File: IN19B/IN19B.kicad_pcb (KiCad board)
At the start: 2 copper layers, 18 x 18 mm, 16 parts

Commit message: Add files via upload
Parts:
- moved H 0.49 mm to (74.0, 106.6), turned to 31 degrees
- moved V 0.27 mm to (72.4, 104.6), turned to 51 degrees
- moved S 0.23 mm to (73.7, 115.2), turned to 321 degrees
- moved F 0.10 mm to (74.8, 113.0), turned to 342 degrees
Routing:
- net Net-(J2-Pad1): track 37.1 -> 11.7 mm
- net Net-(N1-Pad2): track 3.83 -> 0.00 mm
- net Net-(N1-Pad5): track 3.77 -> 0.00 mm
- net Net-(N1-Pad6): track 3.35 -> 0.00 mm
- net Net-(N1-Pad4): track 2.83 -> 0.00 mm

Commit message: Add files via upload
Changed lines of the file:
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@@
     (tags "solder jumper open")
     (attr virtual)
-    (fp_text reference T (at 1.218433 0.100295 218 unlocked) (layer F.SilkS)
+    (fp_text reference T (at 1.218433 0.100295 38 unlocked) (layer F.SilkS)
       (effects (font (size 0.5 0.5) (thickness 0.125)))
     )

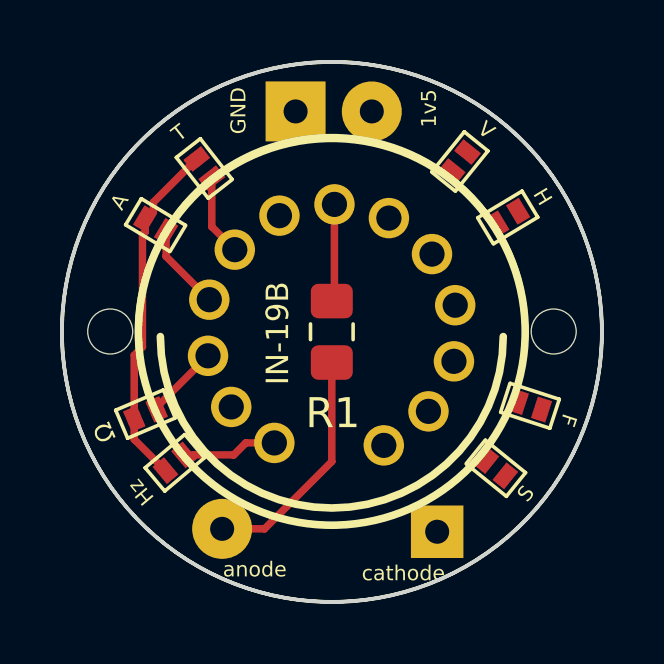
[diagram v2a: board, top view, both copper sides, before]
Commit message: Add files via upload
15 NOV 2020 11:06 PM changed trace width from .25mm to .4 - .75mm.
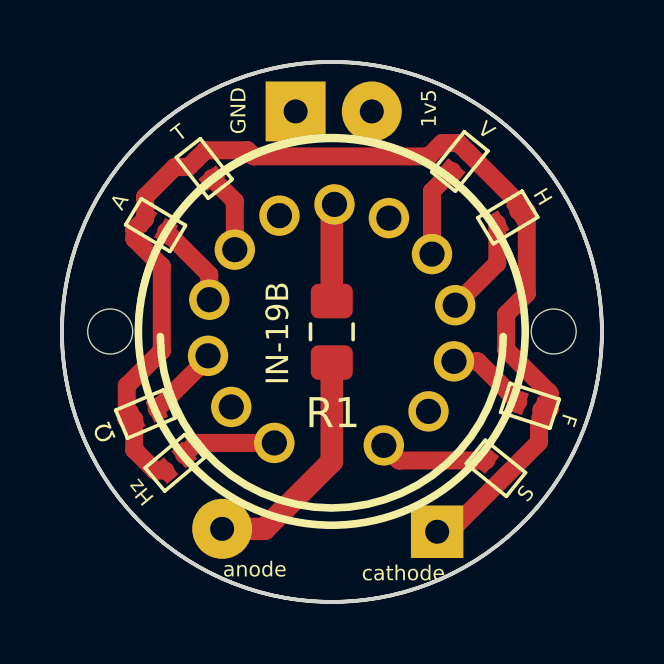
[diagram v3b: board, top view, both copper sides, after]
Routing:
- net Net-(J2-Pad1): track 11.7 -> 38.7 mm
- net Net-(N1-Pad2): track 0.00 -> 3.63 mm
- net Net-(N1-Pad5): track 0.00 -> 3.29 mm
- net Net-(N1-Pad6): track 0.00 -> 3.05 mm
- net Net-(N1-Pad4): track 0.00 -> 2.71 mm
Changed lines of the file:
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@@
     (thickness 1.6)
     (drawings 3)
-    (tracks 27)
+    (tracks 60)
     (zones 0)
     (modules 16)
@@
   )
   (setup
-    (last_trace_width 0.25)
+    (last_trace_width 0.6)
+    (user_trace_width 0.4)
+    (user_trace_width 0.5)
+    (user_trace_width 0.6)
+    (user_trace_width 0.75)
     (trace_clearance 0.2)
     (zone_clearance 0.508)
@@
   (gr_circle (center 68.00342 110.52302) (end 77.00342 110.52302) (layer Edge.Cuts) (width 0.12))
   (gr_circle (center 67.9958 110.5154) (end 76.9958 110.5154) (layer Edge.Cuts) (width 0.12))
-  (segment (start 65.754953 117.08384) (end 64.34074 117.08384) (width 0.25) (layer F.Cu) (net 1))
-  (segment (start 67.9958 114.842993) (end 65.754953 117.08384) (width 0.25) (layer F.Cu) (net 1))
-  (segment (start 67.9958 111.5404) (end 67.9958 114.842993) (width 0.25) (layer F.Cu) (net 1))
-  (segment (start 68.0844 109.4018) (end 67.9958 109.4904) (width 0.25) (layer F.Cu) (net 2))
-  (segment (start 68.0844 106.2683) (end 68.0844 109.4018) (width 0.25) (layer F.Cu) (net 2))
-  (segment (start 63.399631 114.62004) (end 63.07328 114.62004) (width 0.25) (layer F.Cu) (net 3))
-  (segment (start 64.727081 114.62004) (end 63.399631 114.62004) (width 0.25) (layer F.Cu) (net 3))
-  (segment (start 65.127621 114.2195) (end 64.727081 114.62004) (width 0.25) (layer F.Cu) (net 3))
-  (segment (start 66.0808 114.2195) (end 65.127621 114.2195) (width 0.25) (layer F.Cu) (net 3))
-  (segment (start 62.159436 113.026864) (end 63.8702 111.3161) (width 0.25) (layer F.Cu) (net 4))
-  (segment (start 62.159436 113.098865) (end 62.159436 113.026864) (width 0.25) (layer F.Cu) (net 4))
-  (segment (start 62.472423 108.005423) (end 62.472423 107.168157) (width 0.25) (layer F.Cu) (net 5))
-  (segment (start 63.9121 109.4451) (end 62.472423 108.005423) (width 0.25) (layer F.Cu) (net 5))
-  (segment (start 63.99533 107.01103) (end 64.7618 107.7775) (width 0.25) (layer F.Cu) (net 6))
-  (segment (start 63.99533 105.392635) (end 63.99533 107.01103) (width 0.25) (layer F.Cu) (net 6))
-  (segment (start 61.739982 107.222757) (end 61.775718 107.187021) (width 0.25) (layer F.Cu) (net 11))
-  (segment (start 61.41125 114.103109) (end 61.41125 113.416451) (width 0.25) (layer F.Cu) (net 11))
-  (segment (start 62.450639 115.142498) (end 61.41125 114.103109) (width 0.25) (layer F.Cu) (net 11))
-  (segment (start 61.775718 107.187021) (end 61.775718 106.749534) (width 0.25) (layer F.Cu) (net 11))
-  (segment (start 61.684481 111.021241) (end 61.684481 107.278258) (width 0.25) (layer F.Cu) (net 11))
-  (segment (start 61.684481 107.278258) (end 61.775718 107.187021) (width 0.25) (layer F.Cu) (net 11))
-  (segment (start 61.41125 111.294472) (end 61.684481 111.021241) (width 0.25) (layer F.Cu) (net 11))
-  (segment (start 61.41125 113.416451) (end 61.41125 111.294472) (width 0.25) (layer F.Cu) (net 11))
-  (segment (start 63.227764 105.019296) (end 63.49492 104.75214) (width 0.25) (layer F.Cu) (net 11))
-  (segment (start 62.049 106.19806) (end 63.227764 105.019296) (width 0.25) (layer F.Cu) (net 11))
-  (segment (start 62.049 106.476252) (end 62.049 106.19806) (width 0.25) (layer F.Cu) (net 11))
-  (segment (start 61.775718 106.749534) (end 62.049 106.476252) (width 0.25) (layer F.Cu) (net 11))
+  (segment (start 67.9958 112.1154) (end 67.9958 111.5404) (width 0.75) (layer F.Cu) (net 1))
+  (segment (start 67.9958 114.842993) (end 67.9958 112.1154) (width 0.75) (layer F.Cu) (net 1))
+  (segment (start 65.754953 117.08384) (end 67.9958 114.842993) (width 0.75) (layer F.Cu) (net 1))
+  (segment (start 64.34074 117.08384) (end 65.754953 117.08384) (width 0.75) (layer F.Cu) (net 1))
+  (segment (start 67.9958 106.3569) (end 68.0844 106.2683) (width 0.75) (layer F.Cu) (net 2))
+  (segment (start 67.9958 109.4904) (end 67.9958 106.3569) (width 0.75) (layer F.Cu) (net 2))
+  (segment (start 63.47382 114.2195) (end 63.07328 114.62004) (width 0.6) (layer F.Cu) (net 3))
+  (segment (start 66.0808 114.2195) (end 63.47382 114.2195) (width 0.6) (layer F.Cu) (net 3))
+  (segment (start 63.8702 111.388101) (end 62.159436 113.098865) (width 0.6) (layer F.Cu) (net 4))
+  (segment (start 63.8702 111.3161) (end 63.8702 111.388101) (width 0.6) (layer F.Cu) (net 4))
+  (segment (start 63.9121 108.607834) (end 62.472423 107.168157) (width 0.6) (layer F.Cu) (net 5))
+  (segment (start 63.9121 109.4451) (end 63.9121 108.607834) (width 0.6) (layer F.Cu) (net 5))
+  (segment (start 64.7618 106.159105) (end 63.99533 105.392635) (width 0.6) (layer F.Cu) (net 6))
+  (segment (start 64.7618 107.7775) (end 64.7618 106.159105) (width 0.6) (layer F.Cu) (net 6))
+  (segment (start 71.3358 105.826713) (end 72.007581 105.154932) (width 0.6) (layer F.Cu) (net 7))
+  (segment (start 71.3358 107.925) (end 71.3358 105.826713) (width 0.6) (layer F.Cu) (net 7))
+  (segment (start 73.511067 108.227833) (end 73.511067 106.915384) (width 0.6) (layer F.Cu) (net 8))
+  (segment (start 72.1098 109.6291) (end 73.511067 108.227833) (width 0.6) (layer F.Cu) (net 8))
+  (segment (start 72.858799 111.5001) (end 74.21409 112.855391) (width 0.6) (layer F.Cu) (net 9))
+  (segment (start 72.0679 111.5001) (end 72.858799 111.5001) (width 0.6) (layer F.Cu) (net 9))
+  (segment (start 70.234281 114.806581) (end 73.147988 114.806581) (width 0.6) (layer F.Cu) (net 10))
+  (segment (start 69.7291 114.3014) (end 70.234281 114.806581) (width 0.6) (layer F.Cu) (net 10))
+  (segment (start 71.917385 117.18036) (end 73.779652 115.318093) (width 0.6) (layer F.Cu) (net 11))
+  (segment (start 71.50862 117.18036) (end 71.917385 117.18036) (width 0.6) (layer F.Cu) (net 11))
+  (segment (start 74.207772 106.211947) (end 72.519093 104.523268) (width 0.6) (layer F.Cu) (net 11))
+  (segment (start 74.207772 106.496761) (end 74.207772 106.211947) (width 0.6) (layer F.Cu) (net 11))
+  (segment (start 72.252468 104.256643) (end 72.519093 104.523268) (width 0.6) (layer F.Cu) (net 11))
+  (segment (start 72.220465 104.22464) (end 72.252468 104.256643) (width 0.6) (layer F.Cu) (net 11))
+  (segment (start 71.221798 104.669211) (end 71.666369 104.22464) (width 0.6) (layer F.Cu) (net 11))
+  (segment (start 65.389809 104.669211) (end 71.221798 104.669211) (width 0.6) (layer F.Cu) (net 11))
+  (segment (start 71.666369 104.22464) (end 72.220465 104.22464) (width 0.6) (layer F.Cu) (net 11))
+  (segment (start 65.185347 104.464749) (end 65.389809 104.669211) (width 0.6) (layer F.Cu) (net 11))
+  (segment (start 63.782311 104.464749) (end 65.185347 104.464749) (width 0.6) (layer F.Cu) (net 11))
+  (segment (start 63.49492 104.75214) (end 63.782311 104.464749) (width 0.6) (layer F.Cu) (net 11))
+  (segment (start 63.227764 105.019296) (end 62.768024 105.019296) (width 0.6) (layer F.Cu) (net 11))
+  (segment (start 63.49492 104.75214) (end 63.227764 105.019296) (width 0.6) (layer F.Cu) (net 11))
+  (segment (start 61.775718 106.011602) (end 61.775718 106.749534) (width 0.6) (layer F.Cu) (net 11))
+  (segment (start 62.768024 105.019296) (end 61.775718 106.011602) (width 0.6) (layer F.Cu) (net 11))
+  (segment (start 62.450639 115.142498) (end 62.107298 115.142498) (width 0.6) (layer F.Cu) (net 11))
+  (segment (start 61.41125 114.44645) (end 61.41125 113.416451) (width 0.6) (layer F.Cu) (net 11))
+  (segment (start 62.107298 115.142498) (end 61.41125 114.44645) (width 0.6) (layer F.Cu) (net 11))
+  (segment (start 61.139661 113.416451) (end 61.16066 113.395452) (width 0.6) (layer F.Cu) (net 11))
+  (segment (start 61.16066 113.395452) (end 61.16066 112.31626) (width 0.6) (layer F.Cu) (net 11))
+  (segment (start 61.16066 112.31626) (end 62.32906 111.14786) (width 0.6) (layer F.Cu) (net 11))
+  (segment (start 62.32906 108.332026) (end 61.41466 107.417626) (width 0.6) (layer F.Cu) (net 11))
+  (segment (start 62.32906 111.14786) (end 62.32906 108.332026) (width 0.6) (layer F.Cu) (net 11))
+  (segment (start 61.41466 107.110592) (end 61.775718 106.749534) (width 0.6) (layer F.Cu) (net 11))
+  (segment (start 61.41466 107.417626) (end 61.41466 107.110592) (width 0.6) (layer F.Cu) (net 11))
+  (segment (start 74.987109 113.500858) (end 74.90206 113.585907) (width 0.6) (layer F.Cu) (net 11))
+  (segment (start 74.987109 113.10656) (end 74.987109 113.500858) (width 0.6) (layer F.Cu) (net 11))
+  (segment (start 74.90206 114.195685) (end 73.779652 115.318093) (width 0.6) (layer F.Cu) (net 11))
+  (segment (start 74.90206 113.585907) (end 74.90206 114.195685) (width 0.6) (layer F.Cu) (net 11))
+  (segment (start 74.49943 106.496761) (end 74.49566 106.500531) (width 0.6) (layer F.Cu) (net 11))
+  (segment (start 74.49566 106.500531) (end 74.49566 109.24286) (width 0.6) (layer F.Cu) (net 11))
+  (segment (start 74.49566 109.24286) (end 73.80986 109.92866) (width 0.6) (layer F.Cu) (net 11))
+  (segment (start 73.80986 109.92866) (end 73.80986 111.111001) (width 0.6) (layer F.Cu) (net 11))
+  (segment (start 73.80986 111.111001) (end 75.25766 112.558801) (width 0.6) (layer F.Cu) (net 11))
+  (segment (start 75.249974 113.10656) (end 74.987109 113.10656) (width 0.6) (layer F.Cu) (net 11))
+  (segment (start 75.25766 113.098874) (end 75.249974 113.10656) (width 0.6) (layer F.Cu) (net 11))
+  (segment (start 75.25766 112.558801) (end 75.25766 113.098874) (width 0.6) (layer F.Cu) (net 11))
 )
